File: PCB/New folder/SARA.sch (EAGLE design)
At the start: 46 parts, among them U1 MAX9110EKA+T, U2 MAX9110EKA+T, U3 MAX9111EKA+T, U4 MAX9111EKA+T, U5 R-78B3.3-2.0, U6 R-78B3.3-2.0

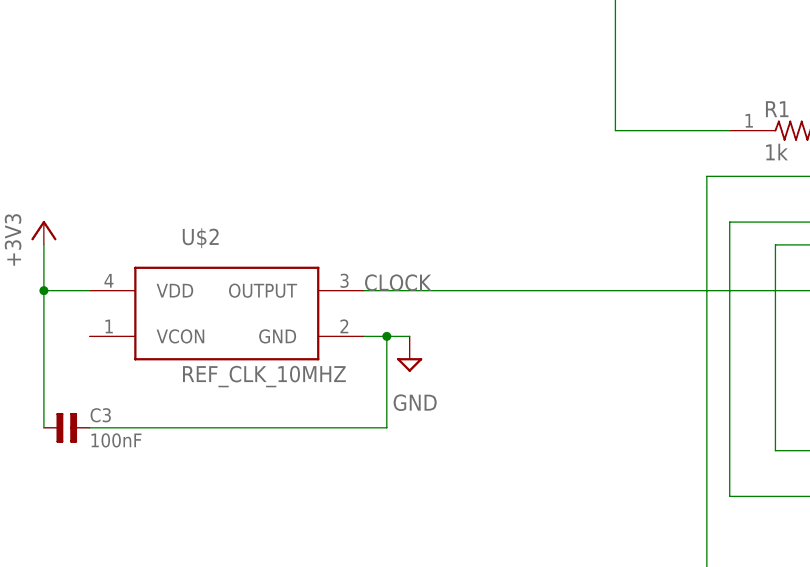
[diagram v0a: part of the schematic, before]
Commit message: 90% done routing, renamed stuff and added differental traces.
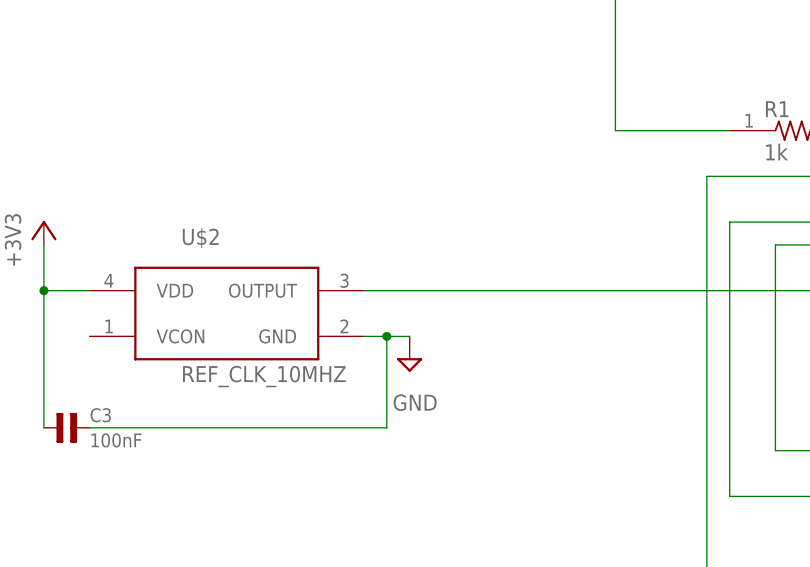
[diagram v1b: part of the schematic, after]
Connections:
- net CLOCK renamed N$6
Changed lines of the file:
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@@
 <class number="0" name="default" width="0" drill="0">
 </class>
-<class number="1" name="Diff" width="0.254" drill="0">
-<clearance class="1" value="0.0508"/>
+<class number="1" name="Diff" width="1.27" drill="0">
+<clearance class="1" value="0.381"/>
 </class>
 </classes>
@@
 </segment>
 </net>
-<net name="CLOCK" class="0">
+<net name="N$6" class="0">
 <segment>
 <pinref part="U$1" gate="G$1" pin="CLOCK"/>
 <pinref part="U$2" gate="G$1" pin="OUTPUT"/>
 <wire x1="10.16" y1="27.94" x2="-53.34" y2="27.94" width="0.1524" layer="91"/>
-<label x="-53.34" y="27.94" size="1.778" layer="95"/>
 </segment>
 </net>
@@
 </segment>
 </net>
-<net name="RXL_P" class="1">
+<net name="RXL_P" class="0">
 <segment>
 <pinref part="SFP_DOWNSTREAM" gate="G$1" pin="RD+"/>
@@
 </segment>
 </net>
-<net name="RXL_N" class="1">
+<net name="RXL_N" class="0">
 <segment>
 <pinref part="SFP_DOWNSTREAM" gate="G$1" pin="RD-"/>
@@
 </segment>
 </net>
-<net name="TXL_N" class="1">
+<net name="TXL_N" class="0">
 <segment>
 <pinref part="SFP_DOWNSTREAM" gate="G$1" pin="TD-"/>
@@
 </segment>
 </net>
-<net name="RXD_P" class="1">
+<net name="RXD_P" class="0">
 <segment>
 <pinref part="U3" gate="G$1" pin="DI+"/>
@@
 </segment>
 </net>
-<net name="RXD_N" class="1">
+<net name="RXD_N" class="0">
 <segment>
 <pinref part="U3" gate="G$1" pin="DI-"/>
@@
 </segment>
 </net>
-<net name="TXD_P" class="1">
+<net name="TXD_P" class="0">
 <segment>
 <pinref part="U1" gate="G$1" pin="DO+"/>
@@
 </segment>
 </net>
-<net name="TXD_N" class="1">
+<net name="TXD_N" class="0">
 <segment>
 <pinref part="U1" gate="G$1" pin="DO-"/>
